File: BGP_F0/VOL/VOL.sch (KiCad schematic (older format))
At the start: 2 parts, among them J1 Conn_01x03

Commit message: F0 Final
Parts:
- removed J1: Conn_01x03, Connectors_JST:JST_PH_B3B-PH-K_03x2.00mm_Straight, symbol Conn_01x03
- added C1: 47n, Capacitors_SMD:C_1206, symbol C_Small
- added P1: CONN_01X02, Connectors_JST:JST_PH_B2B-PH-K_02x2.00mm_Straight, symbol CONN_01X02
- RV1: symbol POT -> POT-RESCUE-VOL
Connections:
- net labels removed: VOL_2
- wire segments 0 -> 2
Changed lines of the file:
@@
 EESchema Schematic File Version 2
+LIBS:VOL-rescue
 LIBS:power
 LIBS:device
 LIBS:switches
 LIBS:relays
-LIBS:motors
 LIBS:transistors
 LIBS:conn
@@
 Comment4 ""
 $EndDescr
-$Comp
-L Conn_01x03 J1
-U 1 1 5A686483
-P 5000 3200
-F 0 "J1" H 5000 3400 50  0000 C CNN
-F 1 "Conn_01x03" H 5000 3000 50  0000 C CNN
-F 2 "Connectors_JST:JST_PH_B3B-PH-K_03x2.00mm_Straight" H 5000 3200 50  0001 C CNN
-F 3 "" H 5000 3200 50  0001 C CNN
-	1    5000 3200
-	-1   0    0    1
-$EndComp
 Text Label 5200 3100 0    60   ~ 0
 VOL_3
 Text Label 5200 3200 0    60   ~ 0
-VOL_2
-Text Label 5200 3300 0    60   ~ 0
 VOL_1
 $Comp
-L POT RV1
+L POT-RESCUE-VOL RV1
 U 1 1 5A6864CE
 P 5800 3200
@@
 	1    0    0    -1
 $EndComp
-Text Label 5800 3350 3    60   ~ 0
+Text Label 5800 3550 3    60   ~ 0
 VOL_3
 Text Label 5800 3050 1    60   ~ 0
 VOL_1
-Text Label 5950 3200 0    60   ~ 0
-VOL_2
+Wire Wire Line
+	5800 3050 5950 3050
+Wire Wire Line
+	5950 3050 5950 3200
+$Comp
+L CONN_01X02 P1
+U 1 1 5A7A6251
+P 5000 3150
+F 0 "P1" H 5000 3300 50  0000 C CNN
+F 1 "CONN_01X02" V 5100 3150 50  0000 C CNN
+F 2 "Connectors_JST:JST_PH_B2B-PH-K_02x2.00mm_Straight" H 5000 3150 50  0001 C CNN
+F 3 "" H 5000 3150 50  0000 C CNN
+	1    5000 3150
+	-1   0    0    1
+$EndComp
+$Comp
+L C_Small C1
+U 1 1 5A7A62B2
+P 5800 3450
+F 0 "C1" H 5810 3520 50  0000 L CNN
+F 1 "47n" H 5810 3370 50  0000 L CNN
+F 2 "Capacitors_SMD:C_1206" H 5800 3450 50  0001 C CNN
+F 3 "" H 5800 3450 50  0000 C CNN
+	1    5800 3450
+	1    0    0    -1
+$EndComp
 $EndSCHEMATC

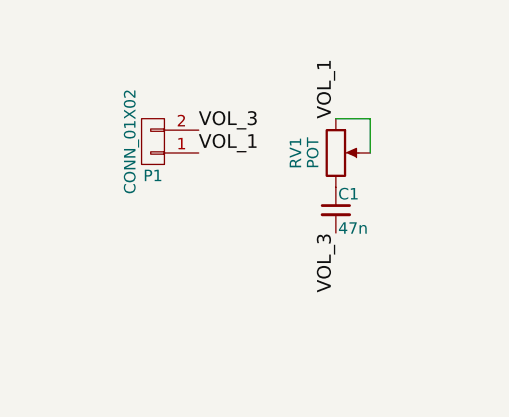
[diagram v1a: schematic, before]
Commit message: Tone cap changed to female pin strip header for 0.047uF and 0.1uF
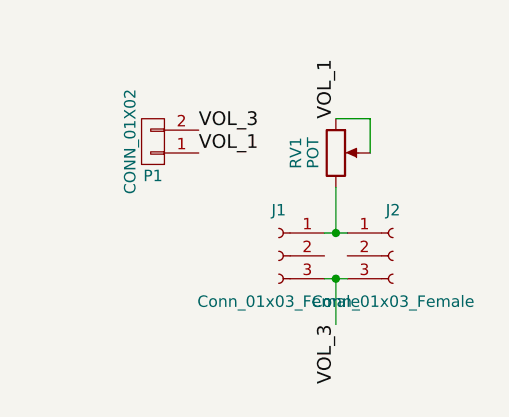
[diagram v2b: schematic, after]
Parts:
- removed C1: 47n, Capacitors_SMD:C_1206, symbol C_Small
- added J1, J2: Conn_01x03_Female, Pin_Headers:Pin_Header_Straight_1x03_Pitch2.54mm, symbol Conn_01x03_Female
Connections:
- net VOL_3: now also J1.3 (Pin_3), J2.3 (Pin_3)
- net at RV1.3: now also J1.1 (Pin_1), J2.1 (Pin_1)
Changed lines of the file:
@@
 EESchema Schematic File Version 2
-LIBS:VOL-rescue
 LIBS:power
 LIBS:device
 LIBS:switches
 LIBS:relays
+LIBS:motors
 LIBS:transistors
 LIBS:conn
@@
 	1    0    0    -1
 $EndComp
-Text Label 5800 3550 3    60   ~ 0
+Text Label 5800 3950 3    60   ~ 0
 VOL_3
 Text Label 5800 3050 1    60   ~ 0
@@
 $EndComp
 $Comp
-L C_Small C1
-U 1 1 5A7A62B2
-P 5800 3450
-F 0 "C1" H 5810 3520 50  0000 L CNN
-F 1 "47n" H 5810 3370 50  0000 L CNN
-F 2 "Capacitors_SMD:C_1206" H 5800 3450 50  0001 C CNN
-F 3 "" H 5800 3450 50  0000 C CNN
-	1    5800 3450
+L Conn_01x03_Female J2
+U 1 1 5A7FCBD4
+P 6050 3650
+F 0 "J2" H 6050 3850 50  0000 C CNN
+F 1 "Conn_01x03_Female" H 6050 3450 50  0000 C CNN
+F 2 "Pin_Headers:Pin_Header_Straight_1x03_Pitch2.54mm" H 6050 3650 50  0001 C CNN
+F 3 "" H 6050 3650 50  0001 C CNN
+	1    6050 3650
 	1    0    0    -1
 $EndComp
+$Comp
+L Conn_01x03_Female J1
+U 1 1 5A7FCBFC
+P 5550 3650
+F 0 "J1" H 5550 3850 50  0000 C CNN
+F 1 "Conn_01x03_Female" H 5550 3450 50  0000 C CNN
+F 2 "Pin_Headers:Pin_Header_Straight_1x03_Pitch2.54mm" H 5550 3650 50  0001 C CNN
+F 3 "" H 5550 3650 50  0001 C CNN
+	1    5550 3650
+	-1   0    0    -1
+$EndComp
+Wire Wire Line
+	5800 3350 5800 3550
+Wire Wire Line
+	5750 3550 5850 3550
+Connection ~ 5800 3550
+Wire Wire Line
+	5750 3750 5850 3750
+Wire Wire Line
+	5800 3750 5800 3950
+Connection ~ 5800 3750
 $EndSCHEMATC

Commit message: Mid Buff
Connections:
- net VOL_1: no longer RV1.2
- net at J1.1 (Pin_1), J2.1 (Pin_1), RV1.3: now also RV1.2
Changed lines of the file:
@@
 Text Label 5800 3050 1    60   ~ 0
 VOL_1
-Wire Wire Line
-	5800 3050 5950 3050
-Wire Wire Line
-	5950 3050 5950 3200
 $Comp
 L CONN_01X02 P1
@@
 	5800 3750 5800 3950
 Connection ~ 5800 3750
+Wire Wire Line
+	5950 3200 5950 3350
+Wire Wire Line
+	5950 3350 5800 3350
 $EndSCHEMATC

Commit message: Tone pot 20k
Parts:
- RV1: footprint LIBS:Potentiometer_Alps_RK097_Single_Vertical -> LIBS:Potentiometer_Alps_RK097_Double_Vertical
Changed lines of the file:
@@
 F 0 "RV1" V 5625 3200 50  0000 C CNN
 F 1 "POT" V 5700 3200 50  0000 C CNN
-F 2 "LIBS:Potentiometer_Alps_RK097_Single_Vertical" H 5800 3200 50  0001 C CNN
+F 2 "LIBS:Potentiometer_Alps_RK097_Double_Vertical" H 5800 3200 50  0001 C CNN
 F 3 "" H 5800 3200 50  0001 C CNN
 	1    5800 3200

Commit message: Various
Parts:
- removed J2: Conn_01x03_Female, Pin_Headers:Pin_Header_Straight_1x03_Pitch2.54mm, symbol Conn_01x03_Female
- added C1: C_Small, Capacitor_THT:C_Rect_L7.2mm_W3.0mm_P5.00mm_FKS2_FKP2_MKS2_MKP2, symbol C_Small
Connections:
- net VOL_3: now also C1.2
- net at J1.1 (Pin_1), RV1.2: now also C1.1; no longer RV1.3
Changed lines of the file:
@@
 EESchema Schematic File Version 2
+LIBS:VOL-rescue
 LIBS:power
 LIBS:device
 LIBS:switches
 LIBS:relays
-LIBS:motors
 LIBS:transistors
 LIBS:conn
@@
 $EndComp
 $Comp
-L Conn_01x03_Female J2
-U 1 1 5A7FCBD4
-P 6050 3650
-F 0 "J2" H 6050 3850 50  0000 C CNN
-F 1 "Conn_01x03_Female" H 6050 3450 50  0000 C CNN
-F 2 "Pin_Headers:Pin_Header_Straight_1x03_Pitch2.54mm" H 6050 3650 50  0001 C CNN
-F 3 "" H 6050 3650 50  0001 C CNN
-	1    6050 3650
-	1    0    0    -1
-$EndComp
-$Comp
 L Conn_01x03_Female J1
 U 1 1 5A7FCBFC
@@
 $EndComp
 Wire Wire Line
-	5800 3350 5800 3550
+	5800 3750 5800 3950
 Wire Wire Line
-	5750 3550 5850 3550
-Connection ~ 5800 3550
+	5950 3550 5950 3200
 Wire Wire Line
-	5750 3750 5850 3750
+	5750 3550 5950 3550
 Wire Wire Line
-	5800 3750 5800 3950
+	5750 3750 5950 3750
+$Comp
+L C_Small C1
+U 1 1 5AF91950
+P 5950 3650
+F 0 "C1" H 5960 3720 50  0000 L CNN
+F 1 "C_Small" H 5960 3570 50  0000 L CNN
+F 2 "Capacitor_THT:C_Rect_L7.2mm_W3.0mm_P5.00mm_FKS2_FKP2_MKS2_MKP2" H 5950 3650 50  0001 C CNN
+F 3 "" H 5950 3650 50  0000 C CNN
+	1    5950 3650
+	1    0    0    -1
+$EndComp
 Connection ~ 5800 3750
-Wire Wire Line
-	5950 3200 5950 3350
-Wire Wire Line
-	5950 3350 5800 3350
 $EndSCHEMATC

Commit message: F0 Tone CTRL
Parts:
- C1: footprint Capacitor_THT:C_Rect_L7.2mm_W3.0mm_P5.00mm_FKS2_FKP2_MKS2_MKP2 -> Capacitors_THT:C_Rect_L7.2mm_W3.0mm_P5.00mm_FKS2_FKP2_MKS2_MKP2
- P1: footprint Connectors_JST:JST_PH_B2B-PH-K_02x2.00mm_Straight -> Pin_Headers:Pin_Header_Straight_1x02_Pitch2.54mm
- RV1: footprint LIBS:Potentiometer_Alps_RK097_Double_Vertical -> LIBS:Potentiometer_Alpha_RV16
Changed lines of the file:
@@
 LIBS:switches
 LIBS:relays
+LIBS:motors
 LIBS:transistors
 LIBS:conn
@@
 F 0 "RV1" V 5625 3200 50  0000 C CNN
 F 1 "POT" V 5700 3200 50  0000 C CNN
-F 2 "LIBS:Potentiometer_Alps_RK097_Double_Vertical" H 5800 3200 50  0001 C CNN
+F 2 "LIBS:Potentiometer_Alpha_RV16" H 5800 3200 50  0001 C CNN
 F 3 "" H 5800 3200 50  0001 C CNN
 	1    5800 3200
@@
 F 0 "P1" H 5000 3300 50  0000 C CNN
 F 1 "CONN_01X02" V 5100 3150 50  0000 C CNN
-F 2 "Connectors_JST:JST_PH_B2B-PH-K_02x2.00mm_Straight" H 5000 3150 50  0001 C CNN
+F 2 "Pin_Headers:Pin_Header_Straight_1x02_Pitch2.54mm" H 5000 3150 50  0001 C CNN
 F 3 "" H 5000 3150 50  0000 C CNN
 	1    5000 3150
@@
 F 0 "C1" H 5960 3720 50  0000 L CNN
 F 1 "C_Small" H 5960 3570 50  0000 L CNN
-F 2 "Capacitor_THT:C_Rect_L7.2mm_W3.0mm_P5.00mm_FKS2_FKP2_MKS2_MKP2" H 5950 3650 50  0001 C CNN
+F 2 "Capacitors_THT:C_Rect_L7.2mm_W3.0mm_P5.00mm_FKS2_FKP2_MKS2_MKP2" H 5950 3650 50  0001 C CNN
 F 3 "" H 5950 3650 50  0000 C CNN
 	1    5950 3650
